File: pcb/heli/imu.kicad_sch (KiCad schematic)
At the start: 3 parts

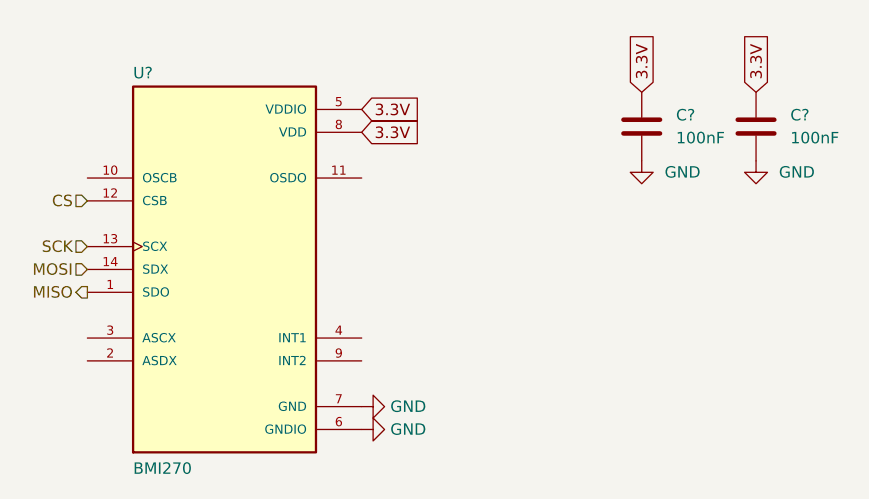
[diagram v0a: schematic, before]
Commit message: Removed MPU6050, updated pcb
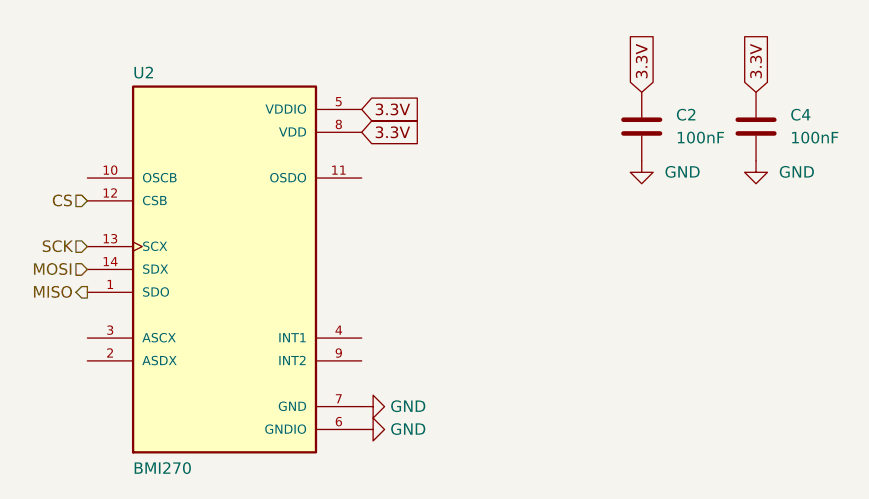
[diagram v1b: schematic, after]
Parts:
- C2, C4: renamed from C?; footprint lib:XDCR_BMI270 -> Capacitor_SMD:C_0603_1608Metric
- gave numbers to parts that had none: 1
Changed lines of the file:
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@@
   (symbol (lib_id "Device:C") (at 120.65 78.74 0) (unit 1)
     (in_bom yes) (on_board yes) (fields_autoplaced)
-    (property "Reference" "C?" (id 0) (at 124.46 77.4699 0)
+    (property "Reference" "C2" (id 0) (at 124.46 77.4699 0)
       (effects (font (size 1.27 1.27)) (justify left))
     )
@@
       (effects (font (size 1.27 1.27)) (justify left))
     )
-    (property "Footprint" "lib:XDCR_BMI270" (id 2) (at 121.6152 82.55 0)
+    (property "Footprint" "Capacitor_SMD:C_0603_1608Metric" (id 2) (at 121.6152 82.55 0)
       (effects (font (size 1.27 1.27)) hide)
     )
@@
   (symbol (lib_id "power:GND") (at 133.35 82.55 0) (unit 1)
     (in_bom yes) (on_board yes) (fields_autoplaced)
-    (property "Reference" "#PWR?" (id 0) (at 133.35 88.9 0)
+    (property "Reference" "#PWR0121" (id 0) (at 133.35 88.9 0)
       (effects (font (size 1.27 1.27)) hide)
     )
@@
   (symbol (lib_id "power:GND") (at 89.535 112.395 90) (unit 1)
     (in_bom yes) (on_board yes) (fields_autoplaced)
-    (property "Reference" "#PWR?" (id 0) (at 95.885 112.395 0)
+    (property "Reference" "#PWR0122" (id 0) (at 95.885 112.395 0)
       (effects (font (size 1.27 1.27)) hide)
     )
@@
   (symbol (lib_id "power:GND") (at 89.535 109.855 90) (unit 1)
     (in_bom yes) (on_board yes) (fields_autoplaced)
-    (property "Reference" "#PWR?" (id 0) (at 95.885 109.855 0)
+    (property "Reference" "#PWR0123" (id 0) (at 95.885 109.855 0)
       (effects (font (size 1.27 1.27)) hide)
     )
@@
   (symbol (lib_id "Device:C") (at 133.35 78.74 0) (unit 1)
     (in_bom yes) (on_board yes) (fields_autoplaced)
-    (property "Reference" "C?" (id 0) (at 137.16 77.4699 0)
+    (property "Reference" "C4" (id 0) (at 137.16 77.4699 0)
       (effects (font (size 1.27 1.27)) (justify left))
     )
@@
       (effects (font (size 1.27 1.27)) (justify left))
     )
-    (property "Footprint" "lib:XDCR_BMI270" (id 2) (at 134.3152 82.55 0)
+    (property "Footprint" "Capacitor_SMD:C_0603_1608Metric" (id 2) (at 134.3152 82.55 0)
       (effects (font (size 1.27 1.27)) hide)
     )
@@
   (symbol (lib_id "lib:BMI270") (at 74.295 94.615 0) (unit 1)
     (in_bom yes) (on_board yes)
-    (property "Reference" "U?" (id 0) (at 64.135 73.533 0)
+    (property "Reference" "U2" (id 0) (at 64.135 73.533 0)
       (effects (font (size 1.27 1.27)) (justify left bottom))
     )
@@
   (symbol (lib_id "power:GND") (at 120.65 82.55 0) (unit 1)
     (in_bom yes) (on_board yes) (fields_autoplaced)
-    (property "Reference" "#PWR?" (id 0) (at 120.65 88.9 0)
+    (property "Reference" "#PWR0120" (id 0) (at 120.65 88.9 0)
       (effects (font (size 1.27 1.27)) hide)
     )

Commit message: Added BMM150 as BMI270 i2c slave
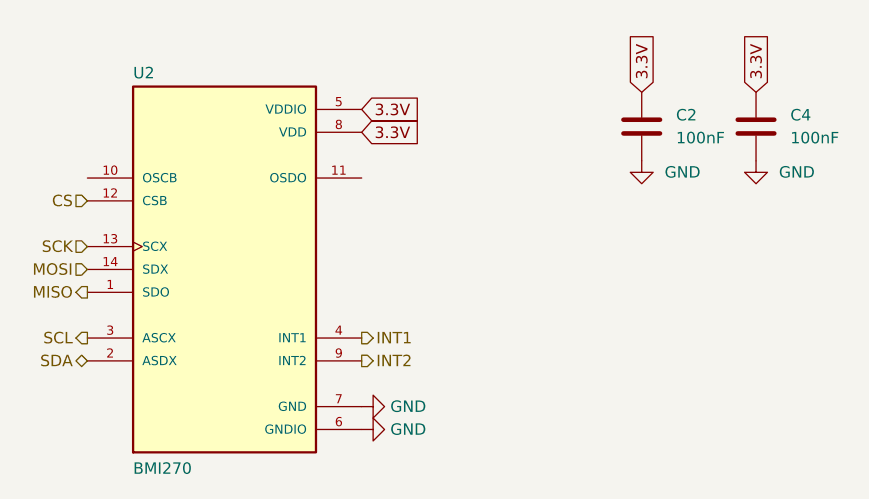
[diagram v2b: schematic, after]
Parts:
- U2: MANUFACTURER Bosch Sensortec -> (none); MAXIMUM_PACKAGE_HEIGHT 0.87mm -> (none); PATREV 1.0 -> (none); STANDARD Manufacturer Recommendations -> (none)
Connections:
- net SDA: now reaches U2.2 (ASDX)
- net SCL: now reaches U2.3 (ASCX)
- net INT1: now reaches U2.4 (INT1)
- net INT2: now reaches U2.9 (INT2)
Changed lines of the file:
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@@
     )
+  )
+  (hierarchical_label "SCL" (shape output) (at 59.055 102.235 180)
+    (effects (font (size 1.27 1.27)) (justify right))
+  )
+  (hierarchical_label "INT1" (shape output) (at 89.535 102.235 0)
+    (effects (font (size 1.27 1.27)) (justify left))
+  )
+  (hierarchical_label "SDA" (shape bidirectional) (at 59.055 104.775 180)
+    (effects (font (size 1.27 1.27)) (justify right))
+  )
+  (hierarchical_label "INT2" (shape output) (at 89.535 104.775 0)
+    (effects (font (size 1.27 1.27)) (justify left))
   )
   (hierarchical_label "SCK" (shape input) (at 59.055 92.075 180)
@@
       (effects (font (size 1.27 1.27)) hide)
     )
-    (property "STANDARD" "Manufacturer Recommendations" (id 4) (at 74.295 94.615 0)
-      (effects (font (size 1.27 1.27)) (justify bottom) hide)
-    )
-    (property "MAXIMUM_PACKAGE_HEIGHT" "0.87mm" (id 5) (at 74.295 94.615 0)
-      (effects (font (size 1.27 1.27)) (justify bottom) hide)
-    )
-    (property "PATREV" "1.0" (id 6) (at 74.295 94.615 0)
-      (effects (font (size 1.27 1.27)) (justify bottom) hide)
-    )
-    (property "MANUFACTURER" "Bosch Sensortec" (id 7) (at 74.295 94.615 0)
-      (effects (font (size 1.27 1.27)) (justify bottom) hide)
-    )
     (property "DIGIKEY" "828-1091-1-ND" (id 8) (at 74.295 94.615 0)
